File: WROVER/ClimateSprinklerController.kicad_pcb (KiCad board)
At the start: 2 copper layers, 136 x 100 mm, 194 parts, among them J1 7.5 TO 40 V, J10 DISPLAY_2, J11 HVAC, J12 RELAY, J2 POWER SEL, J3 EXT_ENC, J4 SERIAL, J5 SPI, J6 I2C, J7 PIR, J8 IO_EXP, J9 DISPLAY_1, K1 G5Q-1-DC5, K2 G5Q-1-DC5, K3 G5Q-1-DC5, Q1 TEPT5700, Q10 2N6073B, Q11 2N6073B, Q12 2N6073B, Q2 2N7002, Q3 2N7002, Q4 2N7002, Q5 2N6073B, Q6 2N6073B, Q7 2N6073B, Q8 2N6073B, Q9 2N6073B, SW1 RESET, SW2 MODE, SW3 PEC11S-929K-S0015, U1 ESP32-WROVER, U10 MOC3043, U11 MOC3043, U12 MOC3043, U13 MOC3043, U14 MOC3043, U15 MOC3043, U16 MOC3043, U17 MOC3043, U2 MCP23017_SO, U3 LMR36520, U4 LD1086DT33TR, U5 SGP40-Sensor_Air_Quality, U6 TMP117, U7 DHT22, U8 BME280, U9 SHTC3

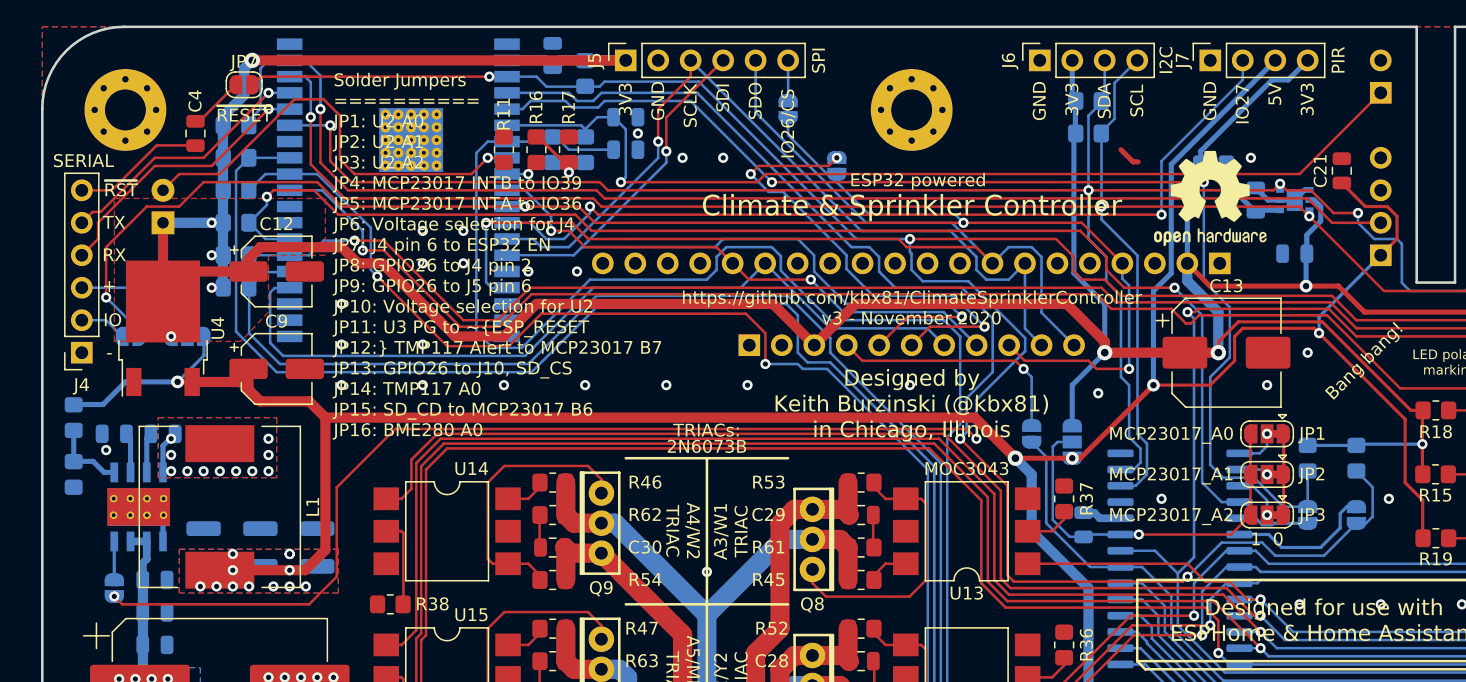
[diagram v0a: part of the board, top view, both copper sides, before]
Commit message: Doc updates, new images, new enclosures, regenerate gerbers
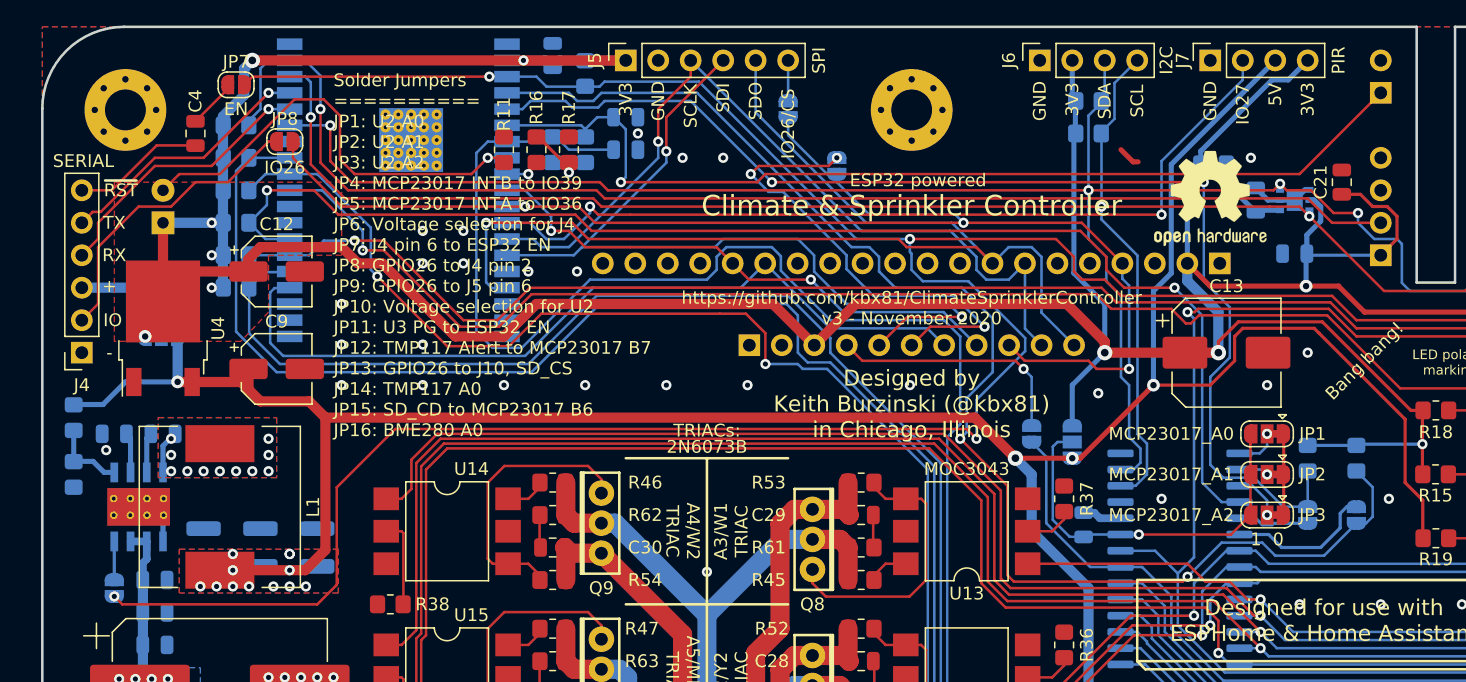
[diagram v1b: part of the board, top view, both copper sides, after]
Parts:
- D1: value CD-MBL206SL -> N/A
- D5, D7, D9: value 1N4148 -> N/A
- F1: value 1.5A -> 300 mA
- JP11: value PG_TO_~RESET -> PG_TO_EN
- JP7: value ~RESET -> EN
- JP8: moved to F.Cu
- R23, R24, R25: value 1K2 -> 560
- R27, R28, R31, R32, R33: value 1K2 -> 1K5
- RV1: value B72205S0400K101 -> N/A
- TH1: value NXFT15XH103FA2B100 -> 10K
- moved JP8 19.4 mm to (101.0, 54.0)
- moved JP6 2.03 mm to (91.3, 69.2)
- moved C21 0.89 mm to (183.6, 57.1)
- moved JP7 0.64 mm to (97.2, 49.5)
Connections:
- C21 pad 1: +5V -> +3V3
- U7 pad 1: +5V -> +3V3
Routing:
- net /DISP_DC: track 130.6 -> 107.9 mm, vias 4 -> 3
- net Net-(J4-Pad2): track 3.69 -> 23.6 mm
- net +5V: track 274.5 -> 256.6 mm, vias 17 -> 16
- net +3V3: track 333.7 -> 348.1 mm, vias 12 -> 13
- net Net-(J4-Pad3): track 10.4 -> 8.71 mm
- net /~ESP_RESET: track 233.5 -> 234.5 mm
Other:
- board text added: "GPI Pull-up resistors"
- board text added: "Solder Jumpers ========== JP1: U2 A0 JP2: U2 A1 JP3: U2 A2 JP4: MCP23017 INTB to IO39 JP5: MCP23017 INTA to IO36 JP6: Voltage selection for J4 JP7: J4 pin 6 to ESP32 EN JP8: GPIO26 to J4 pin 2 JP9: GPIO26 to J5 pin 6 JP10: Voltage selection for U2 JP11: U3 PG to ESP32 EN JP12: TMP117 Alert to MCP23017 B7 JP13: GPIO26 to J10, SD_CS JP14: TMP117 A0 JP15: SD_CD to MCP23017 B6 JP16: BME280 A0"
- board text removed: "GPI 36 & 39 Pull-ups"
- board text removed: "Solder Jumpers ========== JP1: U2 A0 JP2: U2 A1 JP3: U2 A2 JP4: MCP23017 INTB to IO39 JP5: MCP23017 INTA to IO36 JP6: Voltage selection for J4 JP7: J4 pin 6 to ESP32 EN JP8: GPIO26 to J4 pin 2 JP9: GPIO26 to J5 pin 6 JP10: Voltage selection for U2 JP11: U3 PG to ~ESP_RESET JP12: TMP117 Alert to MCP23017 B7 JP13: GPIO26 to J10, SD_CS JP14: TMP117 A0 JP15: SD_CD to MCP23017 B6 JP16: BME280 A0"
